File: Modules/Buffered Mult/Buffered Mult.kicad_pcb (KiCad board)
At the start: 2 copper layers, 50 x 200 mm, 20 parts

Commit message: Testing out gerber generation
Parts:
- H10, H11, H12, H15, H16, H17, H18, H19, H20, H7, H8, H9: footprint SynthStuff:Jack_6.35mm_Cutout_Output_v2 -> SynthStuff:Jack_6.35mm_Cutout_Output_v4

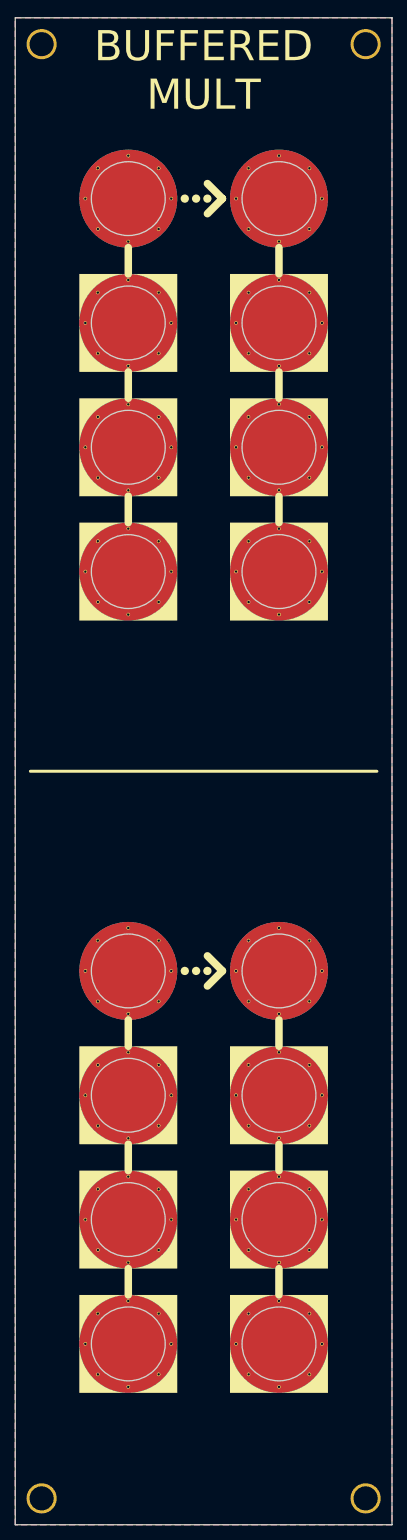
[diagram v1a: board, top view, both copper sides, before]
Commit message: Used jack cutout v5
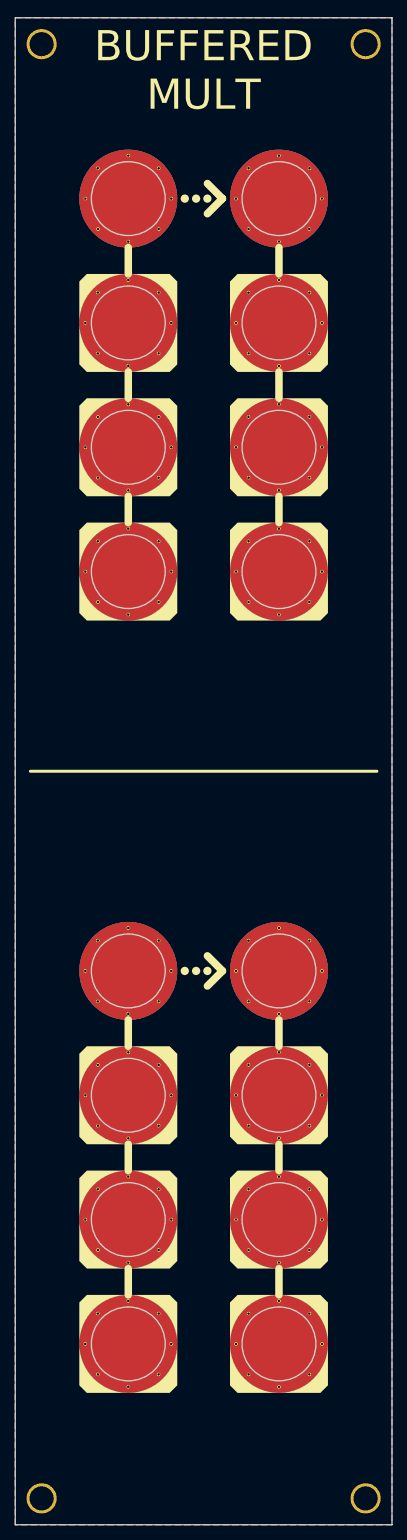
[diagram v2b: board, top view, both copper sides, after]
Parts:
- H10, H11, H12, H15, H16, H17, H18, H19, H20, H7, H8, H9: footprint SynthStuff:Jack_6.35mm_Cutout_Output_v4 -> SynthStuff:Jack_6.35mm_Cutout_Output_v5
